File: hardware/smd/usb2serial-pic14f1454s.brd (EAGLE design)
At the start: 27.9 x 16 mm, 14 parts, among them IC1 PIC16F1454, IC2 TLV760-33, J1 USB-SHIELD-A-H, J2 J2

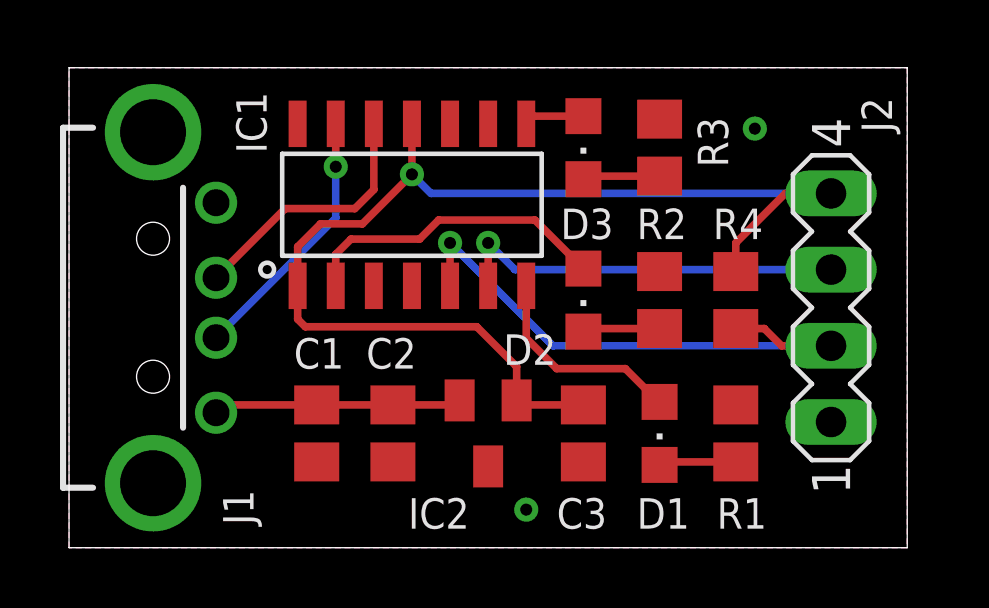
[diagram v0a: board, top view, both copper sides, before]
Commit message: Fixed D+/D- bug
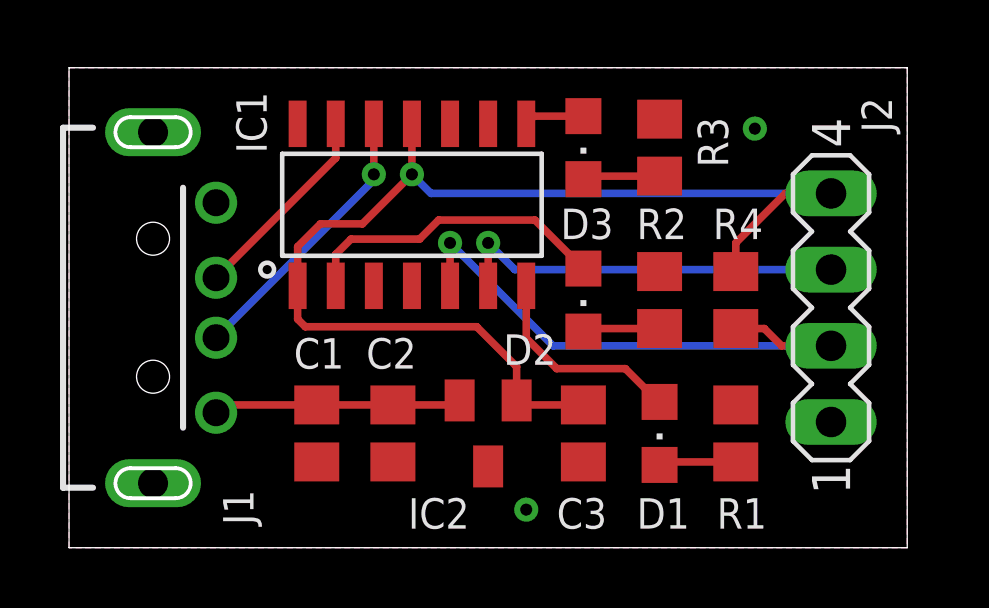
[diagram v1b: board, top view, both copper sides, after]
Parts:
- J1: value USB-SHIELD-A-H -> USB-SHIELD-A-H1; device obddiag-net:USB-A-H -> obddiag-net:USB-A-H1
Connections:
- net N$3: now also IC1.12; no longer IC1.13
- net N$4: now also IC1.13; no longer IC1.12
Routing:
- net N$4: track 8.67 -> 6.78 mm
- net N$3: track 8.78 -> 9.31 mm
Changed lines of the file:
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@@
 <setting verticaltext="up"/>
 </settings>
-<grid distance="0.025" unitdist="inch" unit="mm" style="lines" multiple="1" display="yes" altdistance="0.005" altunitdist="inch" altunit="inch"/>
+<grid distance="0.025" unitdist="inch" unit="mil" style="lines" multiple="1" display="yes" altdistance="0.005" altunitdist="inch" altunit="inch"/>
 <layers>
 <layer number="1" name="Top" color="4" fill="1" visible="yes" active="yes"/>
@@
 <layer number="14" name="Route14" color="1" fill="6" visible="no" active="no"/>
 <layer number="15" name="Route15" color="4" fill="6" visible="no" active="no"/>
-<layer number="16" name="Bottom" color="1" fill="1" visible="yes" active="yes"/>
+<layer number="16" name="Bottom" color="1" fill="1" visible="no" active="yes"/>
 <layer number="17" name="Pads" color="2" fill="1" visible="yes" active="yes"/>
 <layer number="18" name="Vias" color="2" fill="1" visible="yes" active="yes"/>
@@
 <layer number="220" name="220bmp" color="21" fill="1" visible="no" active="no"/>
 <layer number="221" name="221bmp" color="22" fill="1" visible="no" active="no"/>
+<layer number="222" name="222bmp" color="23" fill="1" visible="no" active="no"/>
 <layer number="223" name="223bmp" color="24" fill="1" visible="no" active="no"/>
 <layer number="224" name="224bmp" color="25" fill="1" visible="no" active="no"/>
@@
 </autorouter>
 <elements>
-<element name="J1" library="obddiag-net" package="USB-A-H" value="USB-SHIELD-A-H" x="2.8" y="8" smashed="yes">
+<element name="J1" library="obddiag-net" package="USB-A-H1" value="USB-SHIELD-A-H1" x="2.8" y="8" smashed="yes">
 <attribute name="NAME" x="6.15" y="0.761" size="1.016" layer="25" font="vector" ratio="15" rot="R90"/>
 </element>
@@
 <signal name="N$3">
 <contactref element="J1" pad="D-"/>
-<contactref element="IC1" pad="13"/>
-<wire x1="8.89" y1="14.13" x2="8.89" y2="12.7" width="0.254" layer="1"/>
-<via x="8.89" y="12.7" extent="1-16" drill="0.4"/>
-<wire x1="8.89" y1="12.7" x2="8.89" y2="10.99" width="0.254" layer="16"/>
-<wire x1="8.89" y1="10.99" x2="4.9" y2="7" width="0.254" layer="16"/>
+<via x="10.16" y="12.446" extent="1-16" drill="0.4"/>
+<contactref element="IC1" pad="12"/>
+<wire x1="10.16" y1="14.13" x2="10.16" y2="12.446" width="0.254" layer="1"/>
+<wire x1="10.16" y1="12.446" x2="10.16" y2="12.26" width="0.254" layer="16"/>
+<wire x1="10.16" y1="12.26" x2="4.9" y2="7" width="0.254" layer="16"/>
 </signal>
 <signal name="TX1">
@@
 <wire x1="7.62" y1="10.033" x2="8.382" y2="10.795" width="0.254" layer="1"/>
 <wire x1="8.382" y1="10.795" x2="9.779" y2="10.795" width="0.254" layer="1"/>
-<wire x1="11.43" y1="12.446" x2="11.43" y2="14.13" width="0.254" layer="1"/>
 <wire x1="13.589" y1="7.366" x2="14.92" y2="6.035" width="0.254" layer="1"/>
 <wire x1="7.874" y1="7.366" x2="7.62" y2="7.62" width="0.254" layer="1"/>
@@
 <wire x1="25.4" y1="11.81" x2="12.066" y2="11.81" width="0.254" layer="16"/>
 <wire x1="12.066" y1="11.81" x2="11.43" y2="12.446" width="0.254" layer="16"/>
+<wire x1="11.43" y1="14.13" x2="11.43" y2="12.446" width="0.254" layer="1"/>
 </signal>
 <signal name="N$9">
@@
 <signal name="N$4">
 <contactref element="J1" pad="D+"/>
-<contactref element="IC1" pad="12"/>
-<wire x1="10.16" y1="14.13" x2="10.16" y2="11.938" width="0.254" layer="1"/>
-<wire x1="9.525" y1="11.303" x2="7.203" y2="11.303" width="0.254" layer="1"/>
-<wire x1="7.203" y1="11.303" x2="4.9" y2="9" width="0.254" layer="1"/>
-<wire x1="10.16" y1="11.938" x2="9.525" y2="11.303" width="0.254" layer="1"/>
+<wire x1="8.89" y1="12.99" x2="4.9" y2="9" width="0.254" layer="1"/>
+<contactref element="IC1" pad="13"/>
+<wire x1="8.89" y1="14.13" x2="8.89" y2="12.99" width="0.254" layer="1"/>
 </signal>
 </signals>

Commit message: Minor adjustments
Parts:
- moved C3 0.64 mm to (17.8, 3.81)
- moved D1 0.64 mm to (20.3, 3.81)
- moved D2 0.64 mm to (17.8, 8.26)
- moved D3 0.64 mm to (17.8, 13.3)
- moved J2 0.64 mm to (26.0, 8.00)
- moved R2 0.64 mm to (20.3, 8.26)
- moved R3 0.64 mm to (20.3, 13.3)
- moved R1 0.63 mm to (22.9, 3.81)
- moved R4 0.63 mm to (22.9, 8.26)
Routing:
- net +3V3: track 39.3 -> 40.7 mm
- net TX1: track 13.2 -> 13.9 mm
- net RC2: track 2.01 -> 2.65 mm
- net N$6: track 19.0 -> 19.6 mm
- net RA5: track 10.4 -> 11.1 mm
- net N$9: track 7.07 -> 7.57 mm
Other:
- board size 27.9 x 16 mm -> 28.6 x 16 mm
